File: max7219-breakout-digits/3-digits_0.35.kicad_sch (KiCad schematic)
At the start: 2 parts, among them J1 Conn_02x08_Odd_Even, U1 HDSM-443B_7-Segment_3_Digit

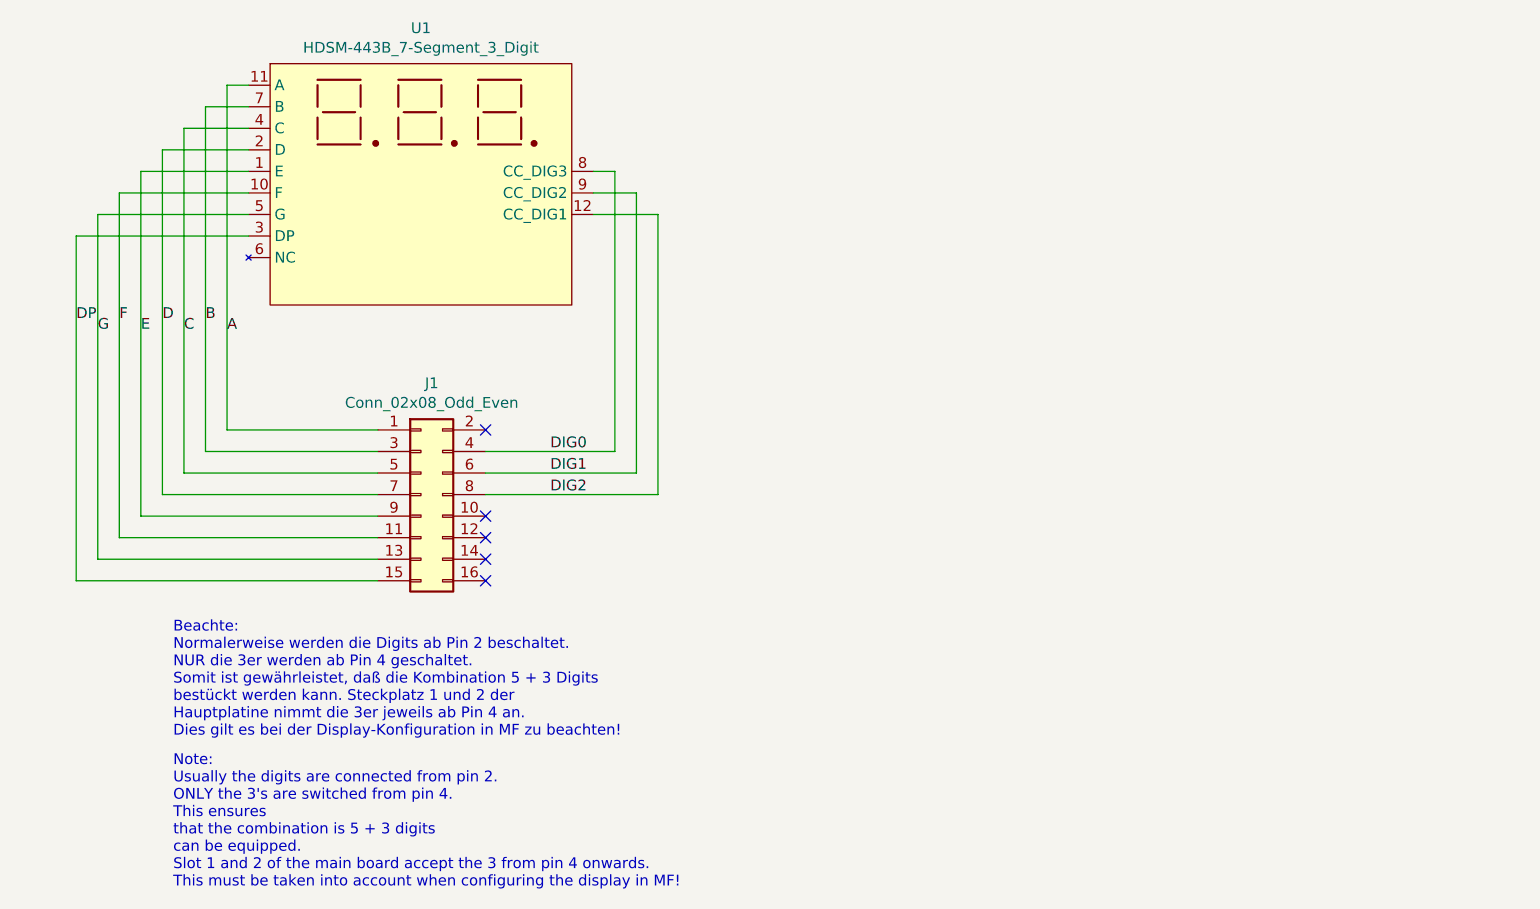
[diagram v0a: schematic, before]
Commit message: add .35 symbols and footprints, rework 3 and 4 digit 0.35
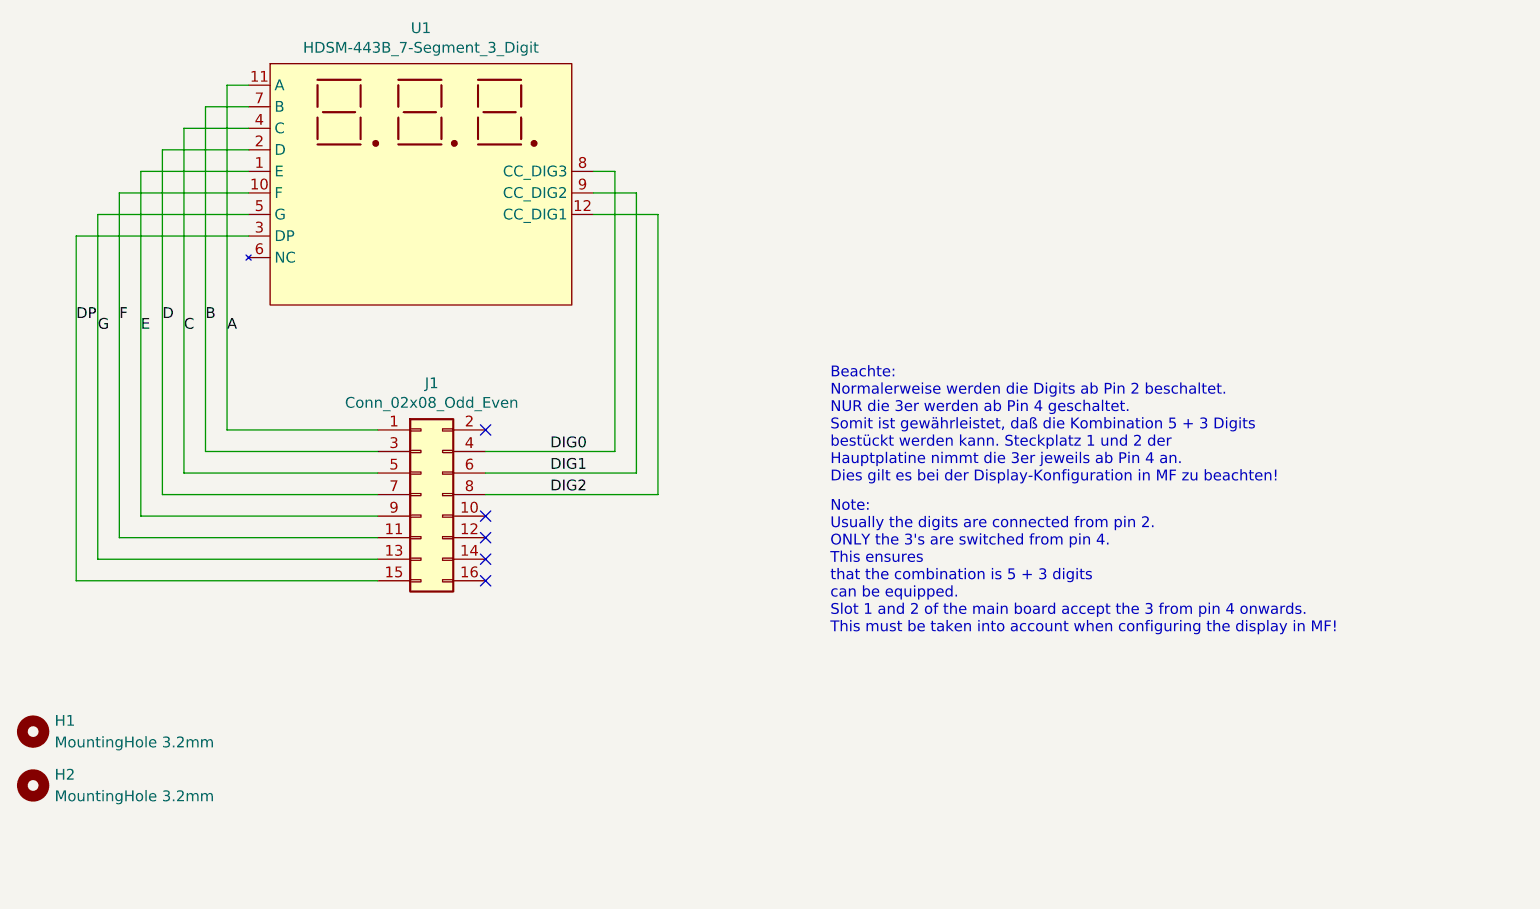
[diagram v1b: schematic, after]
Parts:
- added H1, H2: MountingHole 3.2mm, MountingHole:MountingHole_3.2mm_M3_Pad, symbol MobiFlight:MountingHole 3.2mm
- U1: footprint Display_7Segment:SP42056STH -> MobiFlight:STH_7_3 Digits_0.35_CC; symbol Display_Character:HDSM-443B_7-Segment_3_Digit -> MobiFlight:7Segment 3 digit common cathode STH
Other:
- company: (none) -> MobiFlight
- title: 7-Segment 3 Digits -> 7-Segment Display Module, 3 Digits

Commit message: rotate IDC on 0.28 displays, plated mounting holes for 0.35 displays, set version for 0.35 displays
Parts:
- U1: symbol MobiFlight:7Segment 3 digit common cathode STH -> MobiFlight:7Segment 3 digit 0.35 common cathode STH
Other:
- title: 7-Segment Display Module, 3 Digits -> 7-Segment Display Module 0.35, 3 Digits
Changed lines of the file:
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@@
 	(paper "A5")
 	(title_block
-		(title "7-Segment Display Module, 3 Digits")
+		(title "7-Segment Display Module 0.35, 3 Digits")
 		(date "2025-12")
 		(rev "V5.1")
@@
 	)
 	(symbol
-		(lib_id "MobiFlight:7Segment 3 digit common cathode STH")
+		(lib_id "MobiFlight:7Segment 3 digit 0.35 common cathode STH")
 		(at 71.628 44.704 0)
 		(unit 1)
